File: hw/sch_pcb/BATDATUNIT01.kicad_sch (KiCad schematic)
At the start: 117 parts, among them IC1 MAX14502AETL+, J1 USBC_USB4105-GF-A, J22 HEADER_2x03, J4 46436-9327, J9 SD_Card-FPS009-4200-0, Q1 BC817-25, Q2 BC817-25, Q3 BC817-25, Q4 BC817-25, SW3 KMT031, SW3 SKRTLAE010, SW4 KMT031, SW4 SKRTLAE010, U10 ATMEGA1284P-AU, U11 PCF85263A, U11 TCA4307, U2 USBLC6-2SC6, U3 FT260Q-T, U4 PCA9541ABS/01, U6 AT24CS64-SSHM, U6 SHT35-DIS, U7 TMUX1574DYYR, Y1 19.2 MHz, Y1 8 MHz, Y2 ABS07-120-32.768KHZ-T

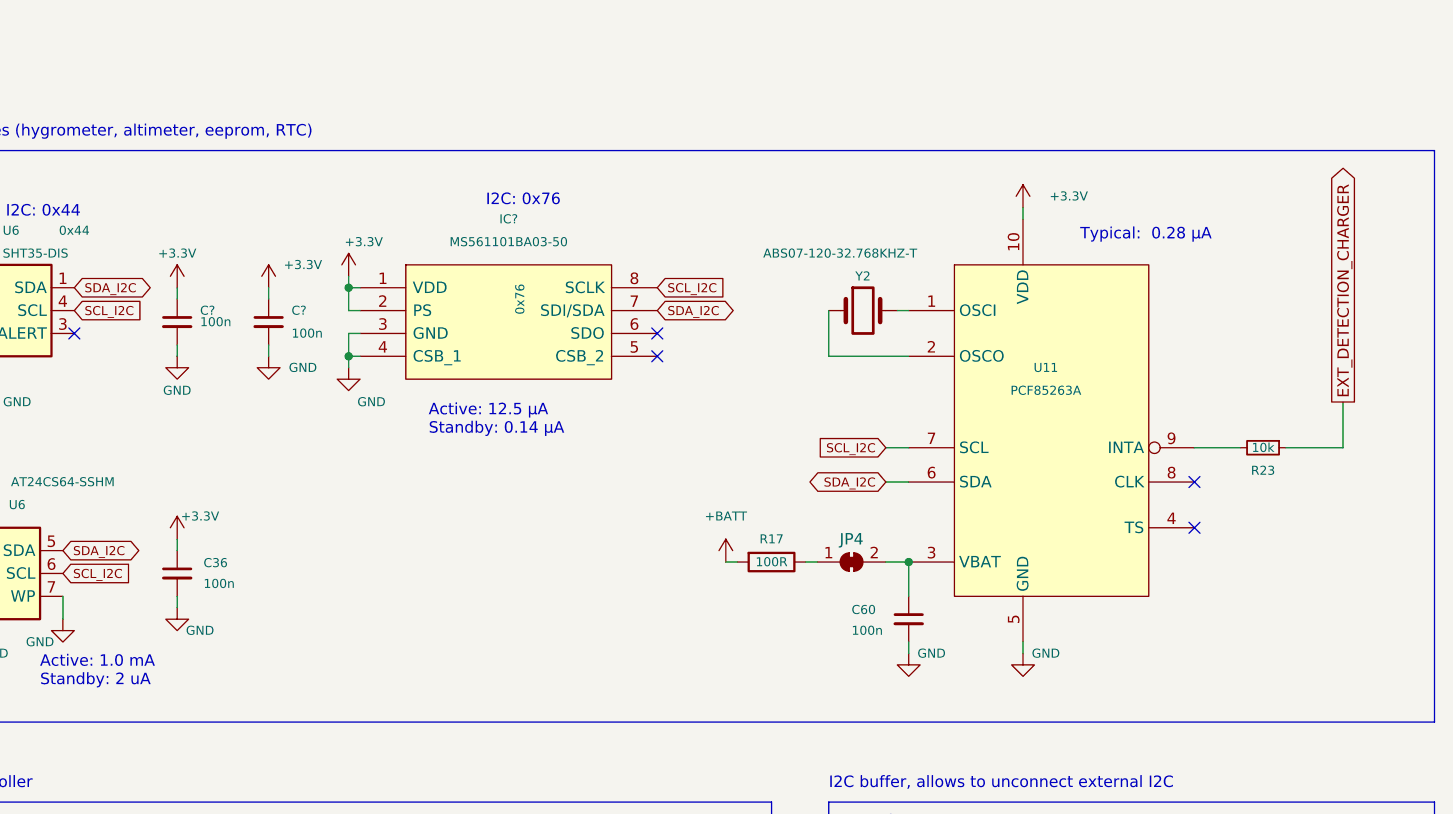
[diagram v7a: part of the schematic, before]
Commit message: Add blocking capacitor to EEPROM.
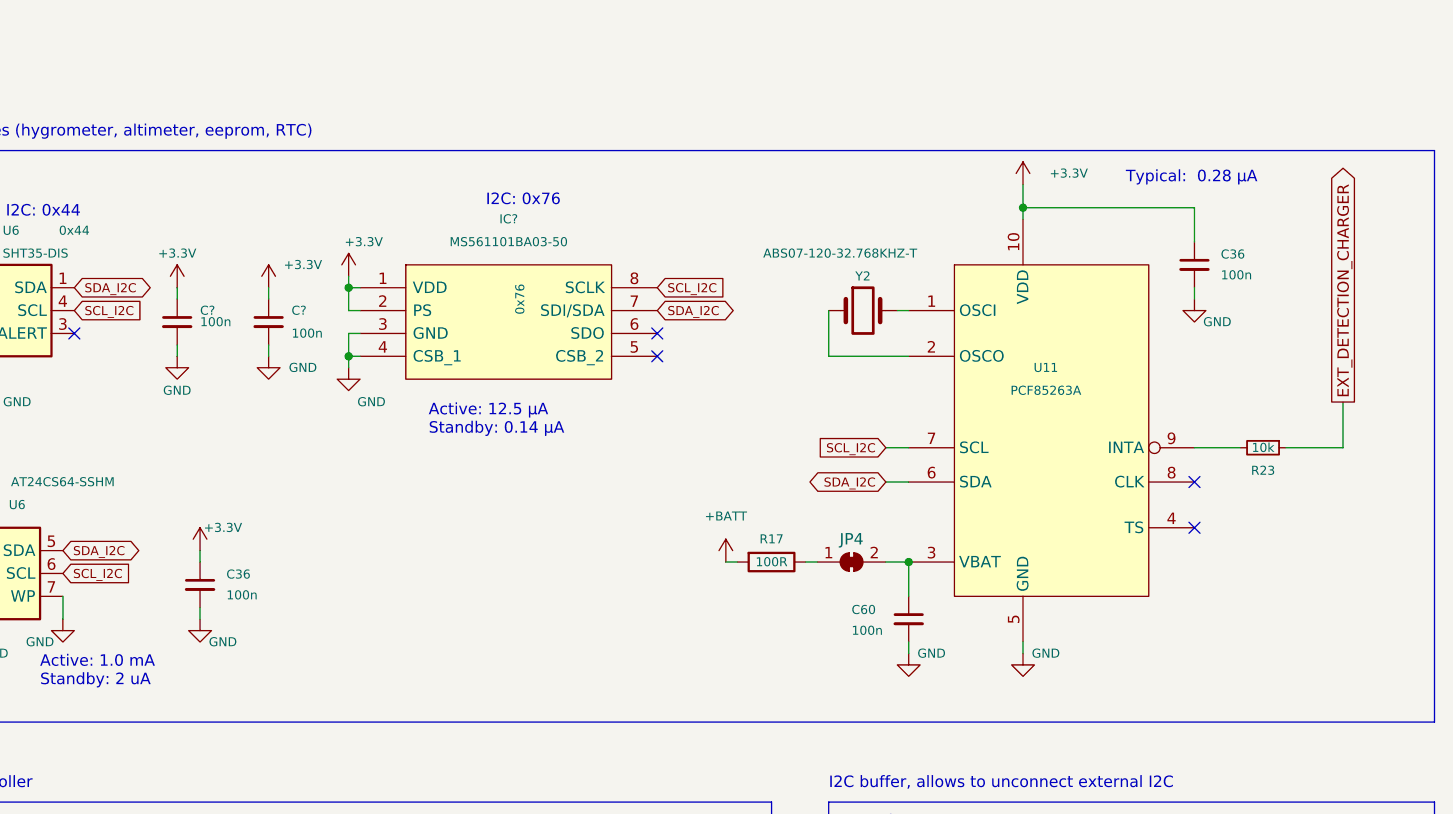
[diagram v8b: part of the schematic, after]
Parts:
- added C36: 100n, Capacitor_SMD:C_0805_2012Metric, symbol Device:C_Small
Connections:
- net +3.3V: now also C36.1
- net GND: now also C36.2
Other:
- moved on the sheet: C36
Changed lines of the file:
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@@
   (junction (at 162.56 35.56) (diameter 0) (color 0 0 0 0)
   )
+  (junction (at 359.41 38.1) (diameter 0) (color 0 0 0 0)
+  )
   (junction (at 360.68 242.57) (diameter 0) (color 0 0 0 0)
   )
@@
     (stroke (width 0) (type default))
   )
+  (wire (pts (xy 359.41 38.1) (xy 359.41 39.37))
+    (stroke (width 0) (type default))
+  )
   (wire (pts (xy 71.12 48.26) (xy 72.39 48.26))
     (stroke (width 0) (type default))
@@
     (stroke (width 0) (type default))
   )
+  (wire (pts (xy 267.97 83.82) (xy 267.97 82.55))
+    (stroke (width 0) (type default))
+  )
   (wire (pts (xy 57.15 38.1) (xy 57.15 35.56))
     (stroke (width 0) (type default))
@@
     (stroke (width 0) (type default))
   )
-  (wire (pts (xy 359.41 38.1) (xy 359.41 39.37))
+  (wire (pts (xy 359.41 35.56) (xy 359.41 38.1))
     (stroke (width 0) (type default))
   )
@@
     (stroke (width 0) (type default))
   )
-  (wire (pts (xy 265.43 74.93) (xy 265.43 76.2))
-    (stroke (width 0) (type default))
-  )
   (wire (pts (xy 140.97 185.42) (xy 146.05 185.42))
     (stroke (width 0) (type default))
@@
     (stroke (width 0) (type default))
   )
+  (wire (pts (xy 378.46 38.1) (xy 378.46 41.91))
+    (stroke (width 0) (type default))
+  )
   (wire (pts (xy 109.22 124.46) (xy 109.22 125.73))
     (stroke (width 0) (type default))
@@
     (stroke (width 0) (type default))
   )
+  (wire (pts (xy 267.97 76.2) (xy 267.97 77.47))
+    (stroke (width 0) (type default))
+  )
   (wire (pts (xy 171.45 144.78) (xy 171.45 147.32))
     (stroke (width 0) (type default))
@@
     (stroke (width 0) (type solid))
   )
+  (wire (pts (xy 359.41 38.1) (xy 378.46 38.1))
+    (stroke (width 0) (type default))
+  )
   (wire (pts (xy 246.38 157.48) (xy 246.38 156.21))
     (stroke (width 0) (type default))
@@
     (stroke (width 0) (type default))
   )
-  (wire (pts (xy 265.43 82.55) (xy 265.43 81.28))
+  (wire (pts (xy 378.46 48.26) (xy 378.46 46.99))
     (stroke (width 0) (type default))
   )
@@
     (effects (font (size 1.27 1.27)) (justify left bottom))
   )
-  (text "Typical:  0.28 μA " (at 365.76 41.91 0)
+  (text "Typical:  0.28 μA " (at 370.84 35.56 0)
     (effects (font (size 1.27 1.27)) (justify left bottom))
   )
@@
     )
   )
-  (symbol (lib_id "Device:C_Small") (at 265.43 78.74 0) (unit 1)
+  (symbol (lib_id "Device:C_Small") (at 378.46 44.45 0) (unit 1)
     (in_bom yes) (on_board yes) (dnp no)
-    (property "Reference" "C36" (at 268.351 77.5716 0)
+    (property "Reference" "C36" (at 381.381 43.2816 0)
       (effects (font (size 1 1)) (justify left))
     )
-    (property "Value" "100n" (at 268.351 79.883 0)
+    (property "Value" "100n" (at 381.381 45.593 0)
       (effects (font (size 1 1)) (justify left))
     )
-    (property "Footprint" "Capacitor_SMD:C_0805_2012Metric" (at 265.43 78.74 0)
+    (property "Footprint" "Capacitor_SMD:C_0805_2012Metric" (at 378.46 44.45 0)
       (effects (font (size 1 1)) hide)
     )
-    (property "Datasheet" "~" (at 265.43 78.74 0)
+    (property "Datasheet" "~" (at 378.46 44.45 0)
       (effects (font (size 1 1)) hide)
     )
-    (property "UST_ID" "5c70984712875079b91f8b4c" (at 265.43 78.74 0)
+    (property "UST_ID" "5c70984712875079b91f8b4c" (at 378.46 44.45 0)
       (effects (font (size 1 1)) hide)
     )
@@
     )
   )
-  (symbol (lib_id "power:GND") (at 265.43 82.55 0) (unit 1)
+  (symbol (lib_id "power:GND") (at 378.46 48.26 0) (unit 1)
     (in_bom yes) (on_board yes) (dnp no)
-    (property "Reference" "#PWR033" (at 265.43 88.9 0)
+    (property "Reference" "#PWR033" (at 378.46 54.61 0)
       (effects (font (size 1 1)) hide)
     )
-    (property "Value" "GND" (at 267.97 85.09 0)
+    (property "Value" "GND" (at 381 50.8 0)
       (effects (font (size 1 1)))
     )
-    (property "Footprint" "" (at 265.43 82.55 0)
+    (property "Footprint" "" (at 378.46 48.26 0)
       (effects (font (size 1 1)) hide)
     )
-    (property "Datasheet" "" (at 265.43 82.55 0)
+    (property "Datasheet" "" (at 378.46 48.26 0)
       (effects (font (size 1 1)) hide)
     )
@@
     )
   )
+  (symbol (lib_id "power:+3.3V") (at 267.97 76.2 0) (unit 1)
+    (in_bom yes) (on_board yes) (dnp no)
+    (property "Reference" "#PWR032" (at 267.97 80.01 0)
+      (effects (font (size 1 1)) hide)
+    )
+    (property "Value" "+3.3V" (at 270.51 73.66 0)
+      (effects (font (size 1 1)))
+    )
+    (property "Footprint" "" (at 267.97 76.2 0)
+      (effects (font (size 1 1)) hide)
+    )
+    (property "Datasheet" "" (at 267.97 76.2 0)
+      (effects (font (size 1 1)) hide)
+    )
+    (pin "1")
+    (instances
+      (project "USTSIPIN02A"
+        (path "/0a87ced0-2af2-43c5-a56c-218f7013d76f/00000000-0000-0000-0000-00005c4aedd8"
+          (reference "#PWR032") (unit 1)
+        )
+      )
+      (project "cpu"
+        (path "/4af4b710-5b7c-4fa3-ad36-3ed9c7e42fc3"
+          (reference "#PWR032") (unit 1)
+        )
+      )
+      (project "BATDATUNIT01"
+        (path "/cca3030a-cb35-4155-89c2-3a41e5a0afad"
+          (reference "#PWR08") (unit 1)
+        )
+      )
+    )
+  )
   (symbol (lib_id "Connector:TestPoint") (at 166.37 143.51 0) (unit 1)
     (in_bom yes) (on_board yes) (dnp no)
@@
     )
   )
-  (symbol (lib_id "power:+3.3V") (at 265.43 74.93 0) (unit 1)
-    (in_bom yes) (on_board yes) (dnp no)
-    (property "Reference" "#PWR032" (at 265.43 78.74 0)
-      (effects (font (size 1 1)) hide)
-    )
-    (property "Value" "+3.3V" (at 267.97 72.39 0)
-      (effects (font (size 1 1)))
-    )
-    (property "Footprint" "" (at 265.43 74.93 0)
-      (effects (font (size 1 1)) hide)
-    )
-    (property "Datasheet" "" (at 265.43 74.93 0)
-      (effects (font (size 1 1)) hide)
-    )
-    (pin "1")
-    (instances
-      (project "USTSIPIN02A"
-        (path "/0a87ced0-2af2-43c5-a56c-218f7013d76f/00000000-0000-0000-0000-00005c4aedd8"
-          (reference "#PWR032") (unit 1)
-        )
-      )
-      (project "cpu"
-        (path "/4af4b710-5b7c-4fa3-ad36-3ed9c7e42fc3"
-          (reference "#PWR032") (unit 1)
-        )
-      )
-      (project "BATDATUNIT01"
-        (path "/cca3030a-cb35-4155-89c2-3a41e5a0afad"
-          (reference "#PWR083") (unit 1)
-        )
-      )
-    )
-  )
   (symbol (lib_id "MLAB_IO:PCF85263A") (at 359.41 62.23 0) (unit 1)
     (in_bom yes) (on_board yes) (dnp no)
@@
     )
   )
+  (symbol (lib_id "Device:C_Small") (at 267.97 80.01 0) (unit 1)
+    (in_bom yes) (on_board yes) (dnp no)
+    (property "Reference" "C36" (at 270.891 78.8416 0)
+      (effects (font (size 1 1)) (justify left))
+    )
+    (property "Value" "100n" (at 270.891 81.153 0)
+      (effects (font (size 1 1)) (justify left))
+    )
+    (property "Footprint" "Capacitor_SMD:C_0805_2012Metric" (at 267.97 80.01 0)
+      (effects (font (size 1 1)) hide)
+    )
+    (property "Datasheet" "~" (at 267.97 80.01 0)
+      (effects (font (size 1 1)) hide)
+    )
+    (property "UST_ID" "5c70984712875079b91f8b4c" (at 267.97 80.01 0)
+      (effects (font (size 1 1)) hide)
+    )
+    (pin "1")
+    (pin "2")
+    (instances
+      (project "USTSIPIN02A"
+        (path "/0a87ced0-2af2-43c5-a56c-218f7013d76f/00000000-0000-0000-0000-00005c4aedd8"
+          (reference "C36") (unit 1)
+        )
+      )
+      (project "cpu"
+        (path "/4af4b710-5b7c-4fa3-ad36-3ed9c7e42fc3"
+          (reference "C36") (unit 1)
+        )
+      )
+      (project "BATDATUNIT01"
+        (path "/cca3030a-cb35-4155-89c2-3a41e5a0afad"
+          (reference "C50") (unit 1)
+        )
+      )
+    )
+  )
   (symbol (lib_id "power:GND") (at 236.22 163.83 0) (unit 1)
     (in_bom yes) (on_board yes) (dnp no)
@@
     )
   )
-  (symbol (lib_id "power:+3.3V") (at 359.41 38.1 0) (unit 1)
+  (symbol (lib_id "power:+3.3V") (at 359.41 35.56 0) (unit 1)
     (in_bom yes) (on_board yes) (dnp no)
-    (property "Reference" "#PWR0143" (at 359.41 41.91 0)
+    (property "Reference" "#PWR0143" (at 359.41 39.37 0)
       (effects (font (size 1 1)) hide)
     )
-    (property "Value" "+3.3V" (at 364.49 36.83 0)
+    (property "Value" "+3.3V" (at 364.49 34.29 0)
       (effects (font (size 1 1)))
     )
-    (property "Footprint" "" (at 359.41 38.1 0)
+    (property "Footprint" "" (at 359.41 35.56 0)
       (effects (font (size 1 1)) hide)
     )
-    (property "Datasheet" "" (at 359.41 38.1 0)
+    (property "Datasheet" "" (at 359.41 35.56 0)
       (effects (font (size 1 1)) hide)
     )
@@
         )
       )
+    )
+  )
+  (symbol (lib_id "power:GND") (at 267.97 83.82 0) (unit 1)
+    (in_bom yes) (on_board yes) (dnp no)
+    (property "Reference" "#PWR033" (at 267.97 90.17 0)
+      (effects (font (size 1 1)) hide)
+    )
+    (property "Value" "GND" (at 270.51 86.36 0)
+      (effects (font (size 1 1)))
+    )
+    (property "Footprint" "" (at 267.97 83.82 0)
+      (effects (font (size 1 1)) hide)
+    )
+    (property "Datasheet" "" (at 267.97 83.82 0)
+      (effects (font (size 1 1)) hide)
+    )
+    (pin "1")
+    (instances
+      (project "USTSIPIN02A"
+        (path "/0a87ced0-2af2-43c5-a56c-218f7013d76f/00000000-0000-0000-0000-00005c4aedd8"
+          (reference "#PWR033") (unit 1)
+        )
+      )
+      (project "cpu"
+        (path "/4af4b710-5b7c-4fa3-ad36-3ed9c7e42fc3"
+          (reference "#PWR033") (unit 1)
+        )
+      )
+      (project "BATDATUNIT01"
+        (path "/cca3030a-cb35-4155-89c2-3a41e5a0afad"
+          (reference "#PWR0174") (unit 1)
+        )
+      )
